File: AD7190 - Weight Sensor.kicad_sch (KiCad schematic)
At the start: 10 parts

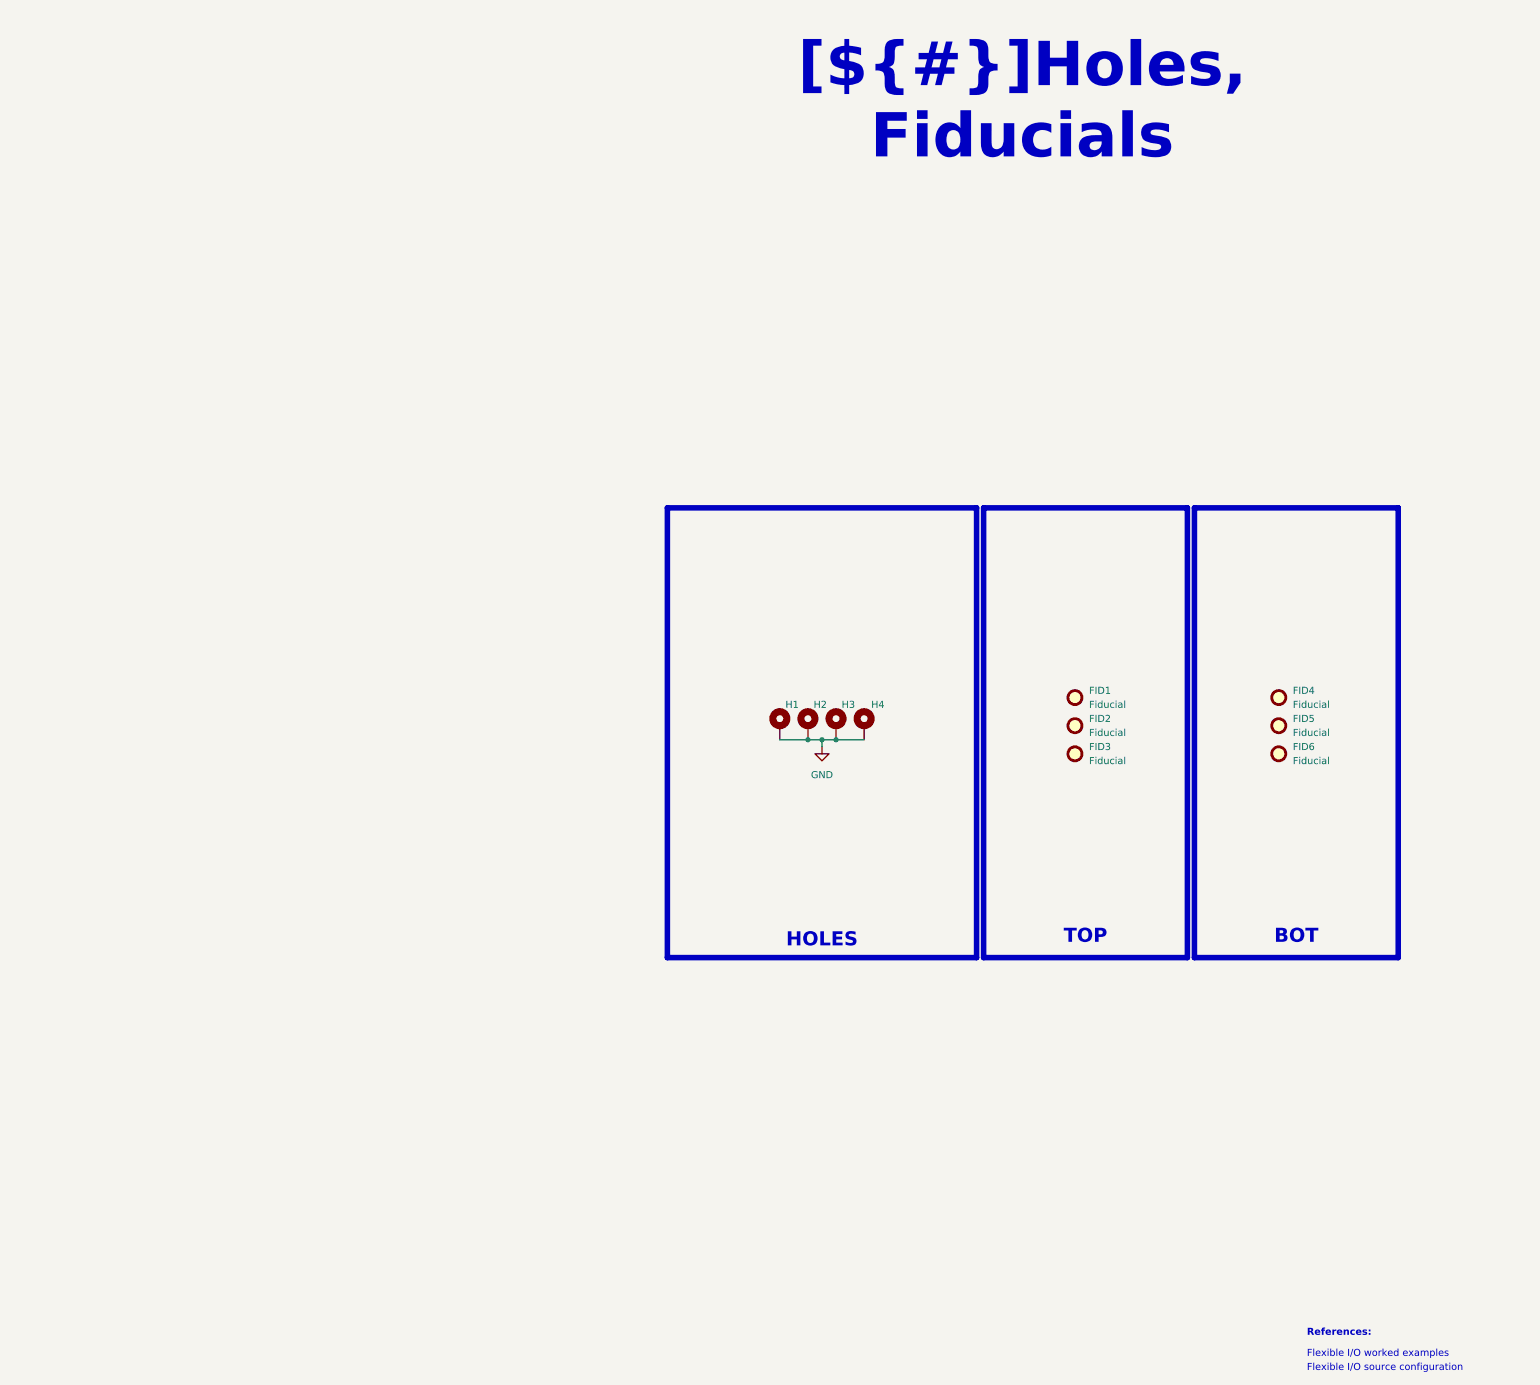
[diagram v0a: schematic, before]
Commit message: Clean up project for KDT template: rename, metadata, KiCad 10 CI
- Rename project Cellule_de_force_V2 -> OPEN_WEIGHT and sheets after their function
  (fix AD7910 -> AD7190 typo), update all sheet/project references in sch/pcb/pro
- Real title-block titles, sheet headers use ${TITLE}, restore KDT drawing sheets,
  remove template leftovers from PCB title block
- kibot_main.yaml: COMPANY = OPEN THRUST LAB, GIT_URL = foukouda/OPEN_WEIGHT
- CI: add KiCad 10 (KiBot v2_dk10), PRELIMINARY variant on dev
- README now generated from kibot_resources/templates/readme.txt; fill CHANGELOG
- Move mechanical CAD to Mechanical/, extend .gitignore, untrack 3Dx logs

Co-Authored-By: Claude Opus 5.5 <noreply@anthropic.com>
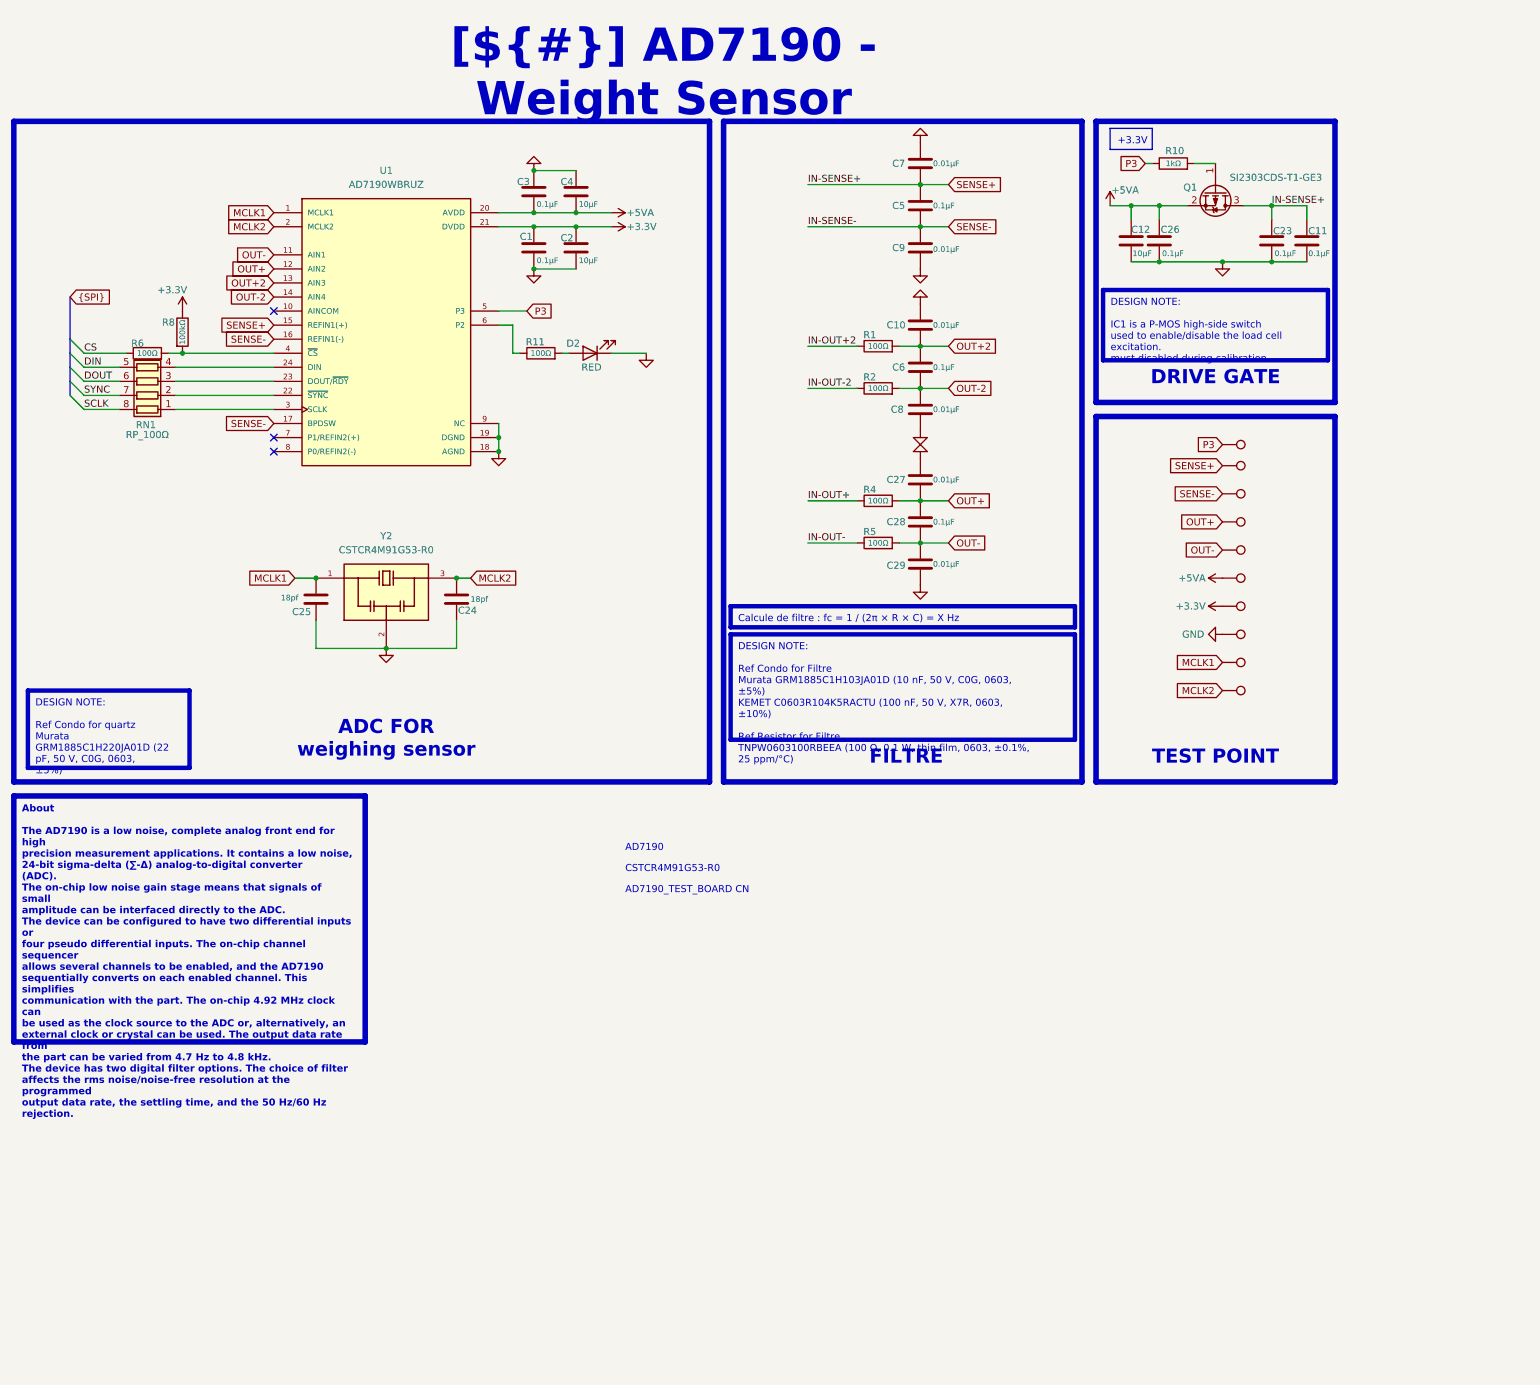
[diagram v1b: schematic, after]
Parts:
- removed FID1, FID2, FID3, FID4, FID5, FID6: Fiducial, Fiducial:Fiducial_1.5mm_Mask3mm, symbol Mechanical:Fiducial
- removed H1, H2, H3, H4: MountingHole_Pad, MountingHole:MountingHole_3.2mm_M3_Pad_Via, symbol Mechanical:MountingHole_Pad
- added C1, C11, C23, C26, C28, C3, C5, C6: 0.1µF, Capacitor_SMD:C_0603_1608Metric, symbol Device:C
- added C10, C27, C29, C7, C8, C9: 0.01µF, Capacitor_SMD:C_0603_1608Metric, symbol Device:C
- added C12, C2, C4: 10µF, Capacitor_SMD:C_0603_1608Metric, symbol Device:C
- added C24, C25: 18pf, Capacitor_SMD:C_0603_1608Metric, symbol Device:C
- added D2: RED, LED_SMD:LED_0603_1608Metric, symbol Device:LED
- added Q1: SI2303CDS-T1-GE3, Package_TO_SOT_SMD:SOT-23-3, symbol Transistor_FET:CSD25480F3
- added R1, R11, R2, R4, R5, R6: 100Ω, Resistor_SMD:R_0603_1608Metric, symbol Device:R
- added R10: 1kΩ, Resistor_SMD:R_0603_1608Metric, symbol Device:R
- added R8: 100kΩ, Resistor_SMD:R_0603_1608Metric, symbol Device:R
- added RN1: RP_100Ω, Resistor_SMD:R_Array_Concave_4x0603, symbol Device:R_Pack04
- added TP1, TP18, TP2, TP3, TP4, TP5, TP6, TP7, TP8, TP9: TestPoint, TestPoint:TestPoint_Pad_D1.5mm, symbol Connector:TestPoint
- added U1: AD7190WBRUZ, AD7190WBRUZ:SOP65P640X120-24N, symbol AD7190WBRUZ:AD7190WBRUZ
- added Y2: CSTCR4M91G53-R0, CSTCR4M91G53-R0:OSC_CSTCR4M91G53-R0, symbol CSTCR4M91G53-R0:CSTCR4M91G53-R0
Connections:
- net GND: now also C1.2, C10.1, C11.2, C12.2, C2.2, C23.2, C24.2, C25.2, C26.2, C27.1, C29.2, C3.1, C4.1, C7.1, C8.2, C9.2, D2.1 (K), TP3.1, U1.18 (AGND), U1.19 (DGND), U1.9 (NC), Y2.2
- new net: R6.2, R8.2, U1.4 (~{CS})
- new net: RN1.1 (R1.1), U1.3 (SCLK)
- new net: RN1.2 (R2.1), U1.22 (~{SYNC})
- new net: RN1.3 (R3.1), U1.23 (DOUT/~{RDY})
- new net: RN1.4 (R4.1), U1.24 (DIN)
- new net: Q1.1 (G), R10.2
- new net: R11.1, U1.6 (P2)
- new net: D2.2 (A), R11.2
- new net +3.3V: C1.1, C2.1, R8.1, TP4.1, U1.21 (DVDD)
- new net +5VA: C12.1, C26.1, C3.2, C4.2, Q1.2 (S), TP5.1, U1.20 (AVDD)
- new net CS: R6.1
- new net DIN: RN1.5 (R4.2)
- new net DOUT: RN1.6 (R3.2)
- new net IN-OUT+: R4.1
- new net IN-OUT+2: R1.1
- new net IN-OUT-: R5.1
- new net IN-OUT-2: R2.1
- new net MCLK1: C25.1, TP2.1, U1.1 (MCLK1), Y2.1
- new net MCLK2: C24.1, TP1.1, U1.2 (MCLK2), Y2.3
- new net OUT+: C27.2, C28.1, R4.2, TP7.1, U1.12 (AIN2)
- new net OUT+2: C10.2, C6.1, R1.2, U1.13 (AIN3)
- new net OUT-: C28.2, C29.1, R5.2, TP6.1, U1.11 (AIN1)
- new net OUT-2: C6.2, C8.1, R2.2, U1.14 (AIN4)
- new net P3: R10.1, TP18.1, U1.5 (P3)
- new net SCLK: RN1.8 (R1.2)
- new net SENSE+: C11.1, C23.1, C5.1, C7.2, Q1.3 (D), TP9.1, U1.15 (REFIN1(+))
- new net SENSE-: C5.2, C9.1, TP8.1, U1.16 (REFIN1(-)), U1.17 (BPDSW)
- new net SYNC: RN1.7 (R2.2)
- no-connect marks 0 -> 3
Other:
- note added: "AD7190"
- note added: "AD7190_TEST_BOARD CN"
- note added: "CSTCR4M91G53-R0"
- note removed: "Flexible I/O source configuration"
- note removed: "Flexible I/O worked examples"
- note removed: "References:"
- title: Sheet Title B -> AD7190 - Weight Sensor

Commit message: Fix load-cell connectivity between Connectors and AD7190 sheets
IN-OUT/IN-SENSE were local labels on two sheets, so the connectors were not
connected to the ADC in the schematic. Convert them to global labels (IN-SENSE
merged into SENSE), and align label polarity on J2/J4 with the routed copper.

Co-Authored-By: Claude Opus 5.5 <noreply@anthropic.com>
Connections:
- net IN-OUT+2: now also R2.1; no longer R1.1
- net IN-OUT-2: now also R1.1; no longer R2.1
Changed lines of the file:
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@@
 		)
 	)
-	(label "IN-SENSE+"
+	(global_label "SENSE+"
+		(shape bidirectional)
 		(at 259.08 45.72 0)
+		(fields_autoplaced yes)
 		(effects
 			(font
 				(size 1.27 1.27)
 			)
-			(justify left bottom)
+			(justify left)
+		)
+		(property "Intersheetrefs" "${INTERSHEET_REFS}"
+			(at 269.0800 45.72 0)
+			(hide yes)
+			(show_name no)
+			(do_not_autoplace no)
+			(effects
+				(font
+					(size 1.27 1.27)
+				)
+				(justify left)
+			)
 		)
 	)
-	(label "IN-SENSE-"
+	(global_label "SENSE-"
+		(shape bidirectional)
 		(at 175.26 49.53 0)
+		(fields_autoplaced yes)
 		(effects
 			(font
 				(size 1.27 1.27)
 			)
-			(justify left bottom)
+			(justify left)
+		)
+		(property "Intersheetrefs" "${INTERSHEET_REFS}"
+			(at 185.2600 49.53 0)
+			(hide yes)
+			(show_name no)
+			(do_not_autoplace no)
+			(effects
+				(font
+					(size 1.27 1.27)
+				)
+				(justify left)
+			)
 		)
 	)
@@
 		)
 	)
-	(label "IN-OUT+2"
+	(global_label "IN-OUT-2"
+		(shape bidirectional)
 		(at 175.26 71.12 0)
+		(fields_autoplaced yes)
 		(effects
 			(font
 				(size 1.27 1.27)
 			)
-			(justify left bottom)
+			(justify left)
+		)
+		(property "Intersheetrefs" "${INTERSHEET_REFS}"
+			(at 185.2600 71.12 0)
+			(hide yes)
+			(show_name no)
+			(do_not_autoplace no)
+			(effects
+				(font
+					(size 1.27 1.27)
+				)
+				(justify left)
+			)
 		)
 	)
-	(label "IN-OUT-2"
+	(global_label "IN-OUT+2"
+		(shape bidirectional)
 		(at 175.26 78.74 0)
+		(fields_autoplaced yes)
 		(effects
 			(font
 				(size 1.27 1.27)
 			)
-			(justify left bottom)
+			(justify left)
+		)
+		(property "Intersheetrefs" "${INTERSHEET_REFS}"
+			(at 185.2600 78.74 0)
+			(hide yes)
+			(show_name no)
+			(do_not_autoplace no)
+			(effects
+				(font
+					(size 1.27 1.27)
+				)
+				(justify left)
+			)
 		)
 	)
@@
 		)
 	)
-	(label "IN-SENSE+"
+	(global_label "SENSE+"
+		(shape bidirectional)
 		(at 175.26 41.91 0)
+		(fields_autoplaced yes)
 		(effects
 			(font
 				(size 1.27 1.27)
 			)
-			(justify left bottom)
+			(justify left)
+		)
+		(property "Intersheetrefs" "${INTERSHEET_REFS}"
+			(at 185.2600 41.91 0)
+			(hide yes)
+			(show_name no)
+			(do_not_autoplace no)
+			(effects
+				(font
+					(size 1.27 1.27)
+				)
+				(justify left)
+			)
 		)
 	)
@@
 		)
 	)
-	(label "IN-OUT+"
+	(global_label "IN-OUT+"
+		(shape bidirectional)
 		(at 175.26 99.06 0)
+		(fields_autoplaced yes)
 		(effects
 			(font
 				(size 1.27 1.27)
 			)
-			(justify left bottom)
+			(justify left)
+		)
+		(property "Intersheetrefs" "${INTERSHEET_REFS}"
+			(at 185.2600 99.06 0)
+			(hide yes)
+			(show_name no)
+			(do_not_autoplace no)
+			(effects
+				(font
+					(size 1.27 1.27)
+				)
+				(justify left)
+			)
 		)
 	)
@@
 		)
 	)
-	(label "IN-OUT-"
+	(global_label "IN-OUT-"
+		(shape bidirectional)
 		(at 175.26 106.68 0)
+		(fields_autoplaced yes)
 		(effects
 			(font
 				(size 1.27 1.27)
 			)
-			(justify left bottom)
+			(justify left)
+		)
+		(property "Intersheetrefs" "${INTERSHEET_REFS}"
+			(at 185.2600 106.68 0)
+			(hide yes)
+			(show_name no)
+			(do_not_autoplace no)
+			(effects
+				(font
+					(size 1.27 1.27)
+				)
+				(justify left)
+			)
 		)
 	)

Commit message: Self-contained libraries, JLCPCB rules, ERC/DRC cleanup
- lib/: project symbol library (19 symbols), footprint library (17 footprints)
  and all 3D models (15), referenced through ${KIPRJMOD} + project lib tables.
  A fresh clone now opens with every symbol, footprint and 3D model.
- Remove duplicated / absolute 3D model paths (C:/Users/..., ${KICAD_FOOTPRINT})
- OPEN_WEIGHT.kicad_dru: JLCPCB 4-layer rules; stackup JLC04161H-7628; board minimums
- AD7190 footprint: drop per-pad 0.102 mm mask margin (mask bridges at 0.65 mm pitch)
- Exclude unplaced TP/FID symbols from board; PWR_FLAGs; decorative wires -> lines
- Local text variables in .kicad_pro; Revision History wired to [Unreleased]
- get_changelog.py: accept "## [Unreleased]" without date
ERC: 0 errors. DRC: 0 errors except 10 courtyard overlaps (placement), 0 parity issues.

Co-Authored-By: Claude Opus 5.5 <noreply@anthropic.com>
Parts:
- C1, C10, C11, C12, C2, C23, C24, C25, C26, C27, C28, C29, C3, C4, C5, C6, C7, C8, C9: footprint Capacitor_SMD:C_0603_1608Metric -> OPEN_WEIGHT:C_0603_1608Metric; symbol Device:C -> OPEN_WEIGHT:C
- D2: footprint LED_SMD:LED_0603_1608Metric -> OPEN_WEIGHT:LED_0603_1608Metric; symbol Device:LED -> OPEN_WEIGHT:LED
- Q1: footprint Package_TO_SOT_SMD:SOT-23-3 -> OPEN_WEIGHT:SOT-23-3; symbol Transistor_FET:CSD25480F3 -> OPEN_WEIGHT:CSD25480F3
- R1, R10, R11, R2, R4, R5, R6, R8: footprint Resistor_SMD:R_0603_1608Metric -> OPEN_WEIGHT:R_0603_1608Metric; symbol Device:R -> OPEN_WEIGHT:R
- RN1: footprint Resistor_SMD:R_Array_Concave_4x0603 -> OPEN_WEIGHT:R_Array_Concave_4x0603; symbol Device:R_Pack04 -> OPEN_WEIGHT:R_Pack04
- TP1, TP3, TP6, TP7, TP8, TP9: footprint TestPoint:TestPoint_Pad_D1.5mm -> OPEN_WEIGHT:TestPoint_Pad_D1.5mm; symbol Connector:TestPoint -> OPEN_WEIGHT:TestPoint; now left out of the parts list
- TP18, TP2, TP4, TP5: footprint TestPoint:TestPoint_Pad_D1.5mm -> OPEN_WEIGHT:TestPoint_Pad_D1.5mm; symbol Connector:TestPoint -> OPEN_WEIGHT:TestPoint
- U1: footprint AD7190WBRUZ:SOP65P640X120-24N -> OPEN_WEIGHT:SOP65P640X120-24N; symbol AD7190WBRUZ:AD7190WBRUZ -> OPEN_WEIGHT:AD7190WBRUZ
- Y2: footprint CSTCR4M91G53-R0:OSC_CSTCR4M91G53-R0 -> OPEN_WEIGHT:OSC_CSTCR4M91G53-R0; symbol CSTCR4M91G53-R0:CSTCR4M91G53-R0 -> OPEN_WEIGHT:CSTCR4M91G53-R0
